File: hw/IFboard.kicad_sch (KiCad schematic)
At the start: 104 parts, among them J1 USB_C_Receptacle_USB2.0_16P, J10 IcoTec_36650.2, J2 Conn_01x03_Socket, J3 Conn_ARM_SWD_TagConnect_TC203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, J4 Conn_01x03_Socket, J5 Conn_01x03_Socket, J6 Conn_01x03_Socket, J7 IcoTec_36650.2, J8 IcoTec_36650.2, J9 IcoTec_36650.2, SW3 SW_Push, SW4 SW_Push, SW5 SW_Push, SW6 SW_Push, U1 AMS1117-3.3, U2 XC6206P332MR-G, U3 TCAN3413DR, U4 ST4E1240DT, U5 MAX232ESE+T, U6 STM32G0B1CBTx, U7 ER_OLEDM0.91_1x-I2C

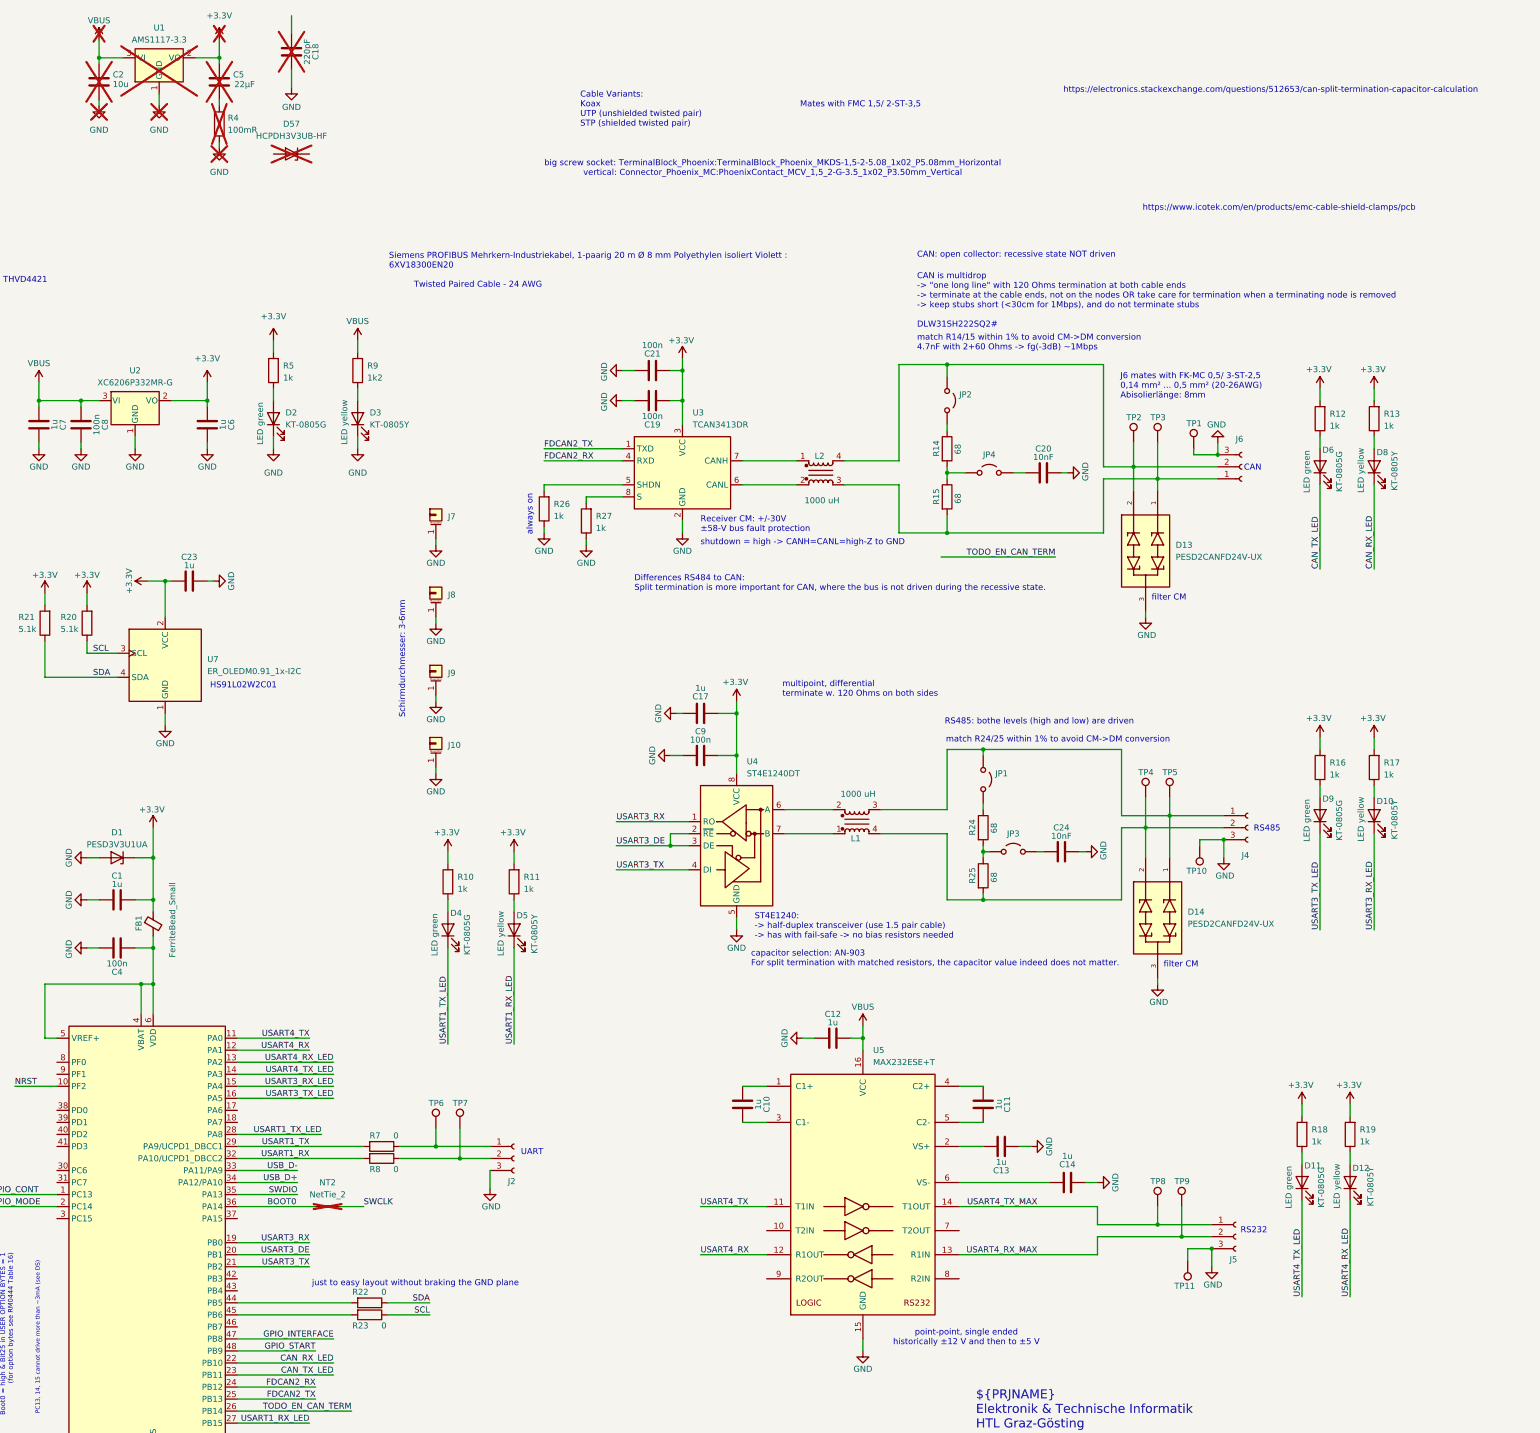
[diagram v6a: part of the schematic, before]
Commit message: modified connectors to vertical
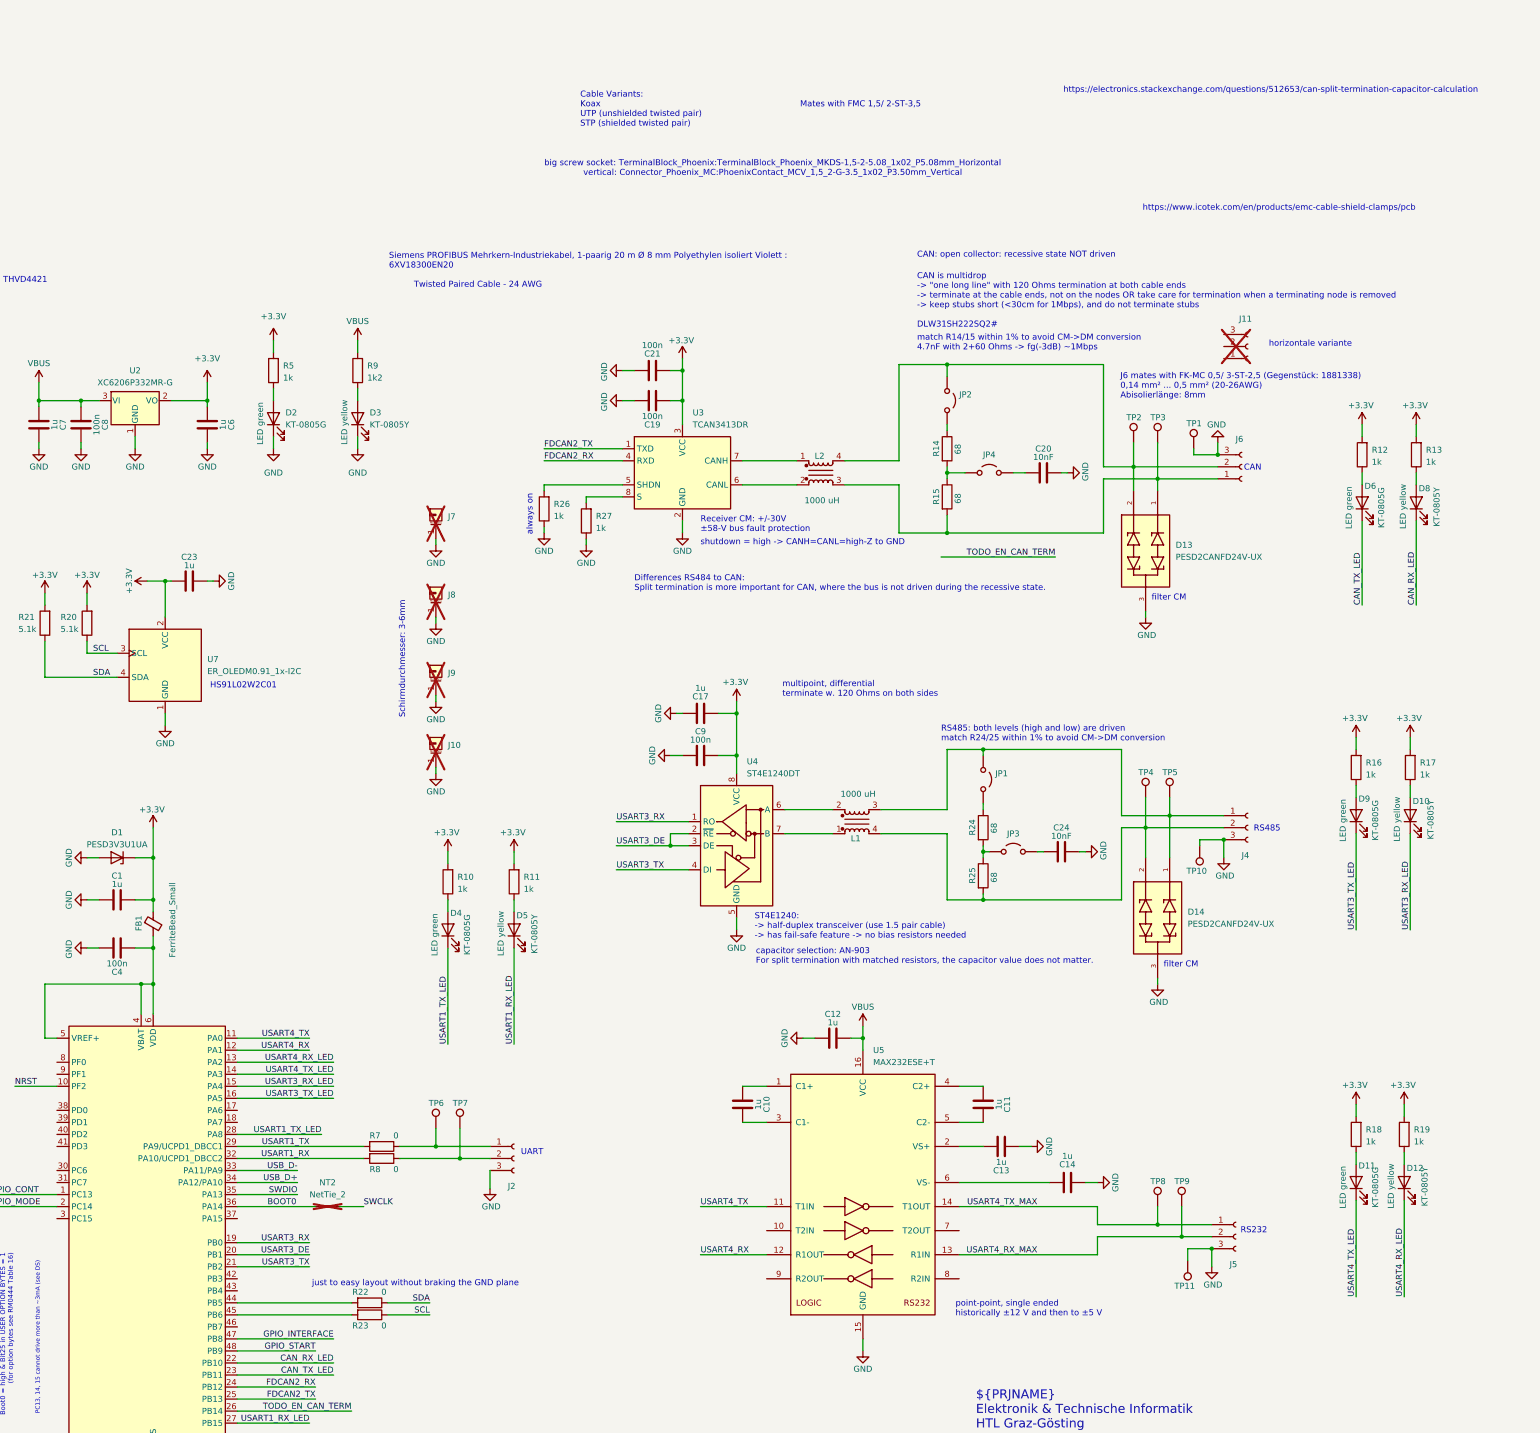
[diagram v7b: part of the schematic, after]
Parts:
- removed C18: 220pF, Capacitor_SMD:C_0402_1005Metric, symbol Device:C
- removed C2: 10u, Capacitor_SMD:C_0805_2012Metric, symbol Device:C
- removed C5: 22µF, Capacitor_SMD:C_0805_2012Metric, symbol Device:C
- removed D57: HCPDH3V3UB-HF, Diode_SMD:D_SOD-523, symbol Diode:PESD5V0L1UL
- removed R4: 100mR, Resistor_SMD:R_1206_3216Metric, symbol Device:R
- removed U1: AMS1117-3.3, Package_TO_SOT_SMD:SOT-223-3_TabPin2, symbol Regulator_Linear:AMS1117-3.3
- added J11: Conn_01x03_Socket, PZL:1881451, symbol Connector:Conn_01x03_Socket
- D7: now in the parts list
- J10, J7, J8, J9: now not fitted
- J2, J4, J5, J6: value Conn_01x03_Socket -> Phoenix_1881561; footprint PZL:1881451 -> PZ:1881561; symbol Connector:Conn_01x03_Socket -> PZ:Phoenix_1881561; LCSC Part # (none) -> C3585554
- L1, L2: LCSC Part # (none) -> C2651122
- TP2, TP3, TP4, TP5, TP6, TP7, TP8, TP9: footprint TestPoint:TestPoint_Keystone_5005-5009_Compact -> PZ:TP_Keystone_5010-5014_Multipurpose; LCSC Part # (none) -> C2906765
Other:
- note added: "J6 mates with FK-MC 0,5/ 3-ST-2,5 (Gegenstück: 1881338) 0,14 mm² ... 0,5 mm² (20-26AWG) Abisolierlänge: 8mm"
- note added: "RS485: both levels (high and low) are driven match R24/25 within 1% to avoid CM->DM conversion"
- note added: "ST4E1240: -> half-duplex transceiver (use 1.5 pair cable) -> has fail-safe feature -> no bias resistors needed"
- note added: "capacitor selection: AN-903 For split termination with matched resistors, the capacitor value does not matter."
- note added: "horizontale variante"
- note removed: "J6 mates with FK-MC 0,5/ 3-ST-2,5 0,14 mm² ... 0,5 mm² (20-26AWG) Abisolierlänge: 8mm"
- note removed: "RS485: bothe levels (high and low) are driven"
- note removed: "ST4E1240: -> half-duplex transceiver (use 1.5 pair cable) -> has with fail-safe -> no bias resistors needed"
- note removed: "capacitor selection: AN-903 For split termination with matched resistors, the capacitor value indeed does not matter."
- note removed: "match R24/25 within 1% to avoid CM->DM conversion"
- moved on the sheet: D10, D11, D12, D6, D8, D9, R12, R13, R16, R17, R18, R19

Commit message: cleanup
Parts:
- D13, D14: footprint PZL:TVS_PESD2CANFD24V-UX -> PZ:TVS_PESD2CANFD24V-UX; symbol newLib:PESD2CANFD24V-UX -> PZ:PESD2CANFD24V-UX
- J10, J7, J8, J9: now fitted
- J11: value Conn_01x03_Socket -> MC_0,5/_3-G-2,5; footprint PZL:1881451 -> PZ:1881451; symbol Connector:Conn_01x03_Socket -> PZ:MC_0,5/_3-G-2,5
- JP1, JP2, JP3, JP4: now not fitted
- L1, L2: footprint PZL:L_Wurth_WE-SL2-74422x -> PZ:L_Wurth_WE-SL2-74422x; symbol newLib:74422x_744222 -> PZ:74422x_744222
- NT2: footprint Franz:R_0402_1005Metric_solderjmp_short -> PZ:R_0402_1005Metric_solderjmp_short; now fitted
- TP1, TP10, TP11: value TestPoint -> TestPoint_Keystone_5019; footprint PZL:TestPoint_Keystone_5019_Miniature -> PZ:TestPoint_Keystone_5019_Miniature; symbol Connector:TestPoint -> PZ:TestPoint_Keystone_5019; LCSC Part # (none) -> C238131
- U7: footprint PZL:ER_OLEDM0.91_1x-I2C -> PZ:ER_OLEDM0.91_1x-I2C; symbol Display_Graphic:ER_OLEDM0.91_1x-I2C -> PZ:ER_OLEDM0.91_1x-I2C
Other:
- note added: "CMC: https://www.ti.com/lit/an/slla271/slla271.pdf"
- note added: "Diverses: big screw socket: TerminalBlock_Phoenix:TerminalBlock_Phoenix_MKDS-1,5-2-5.08_1x02_P5.08mm_Horizontal vertical: Connector_Phoenix_MC:PhoenixContact_MCV_1,5_2-G-3.5_1x02_P3.50mm_Vertical"
- note removed: "Mates with FMC 1,5/ 2-ST-3,5"
- note removed: "big screw socket: TerminalBlock_Phoenix:TerminalBlock_Phoenix_MKDS-1,5-2-5.08_1x02_P5.08mm_Horizontal vertical: Connector_Phoenix_MC:PhoenixContact_MCV_1,5_2-G-3.5_1x02_P3.50mm_Vertical"
- moved on the sheet: C20, D13, J11, J6, R14, R15, TP1, TP2, TP3
